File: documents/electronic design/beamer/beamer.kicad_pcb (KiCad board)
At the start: 2 copper layers, 28 parts, among them P1 CONN_01X20, P2 CONN_01X20, P3 CONN_01X02, P4 CONN_01X01, P5 CONN_01X01, T1 2N7002K, T10 2N7002K, T2 2N7002K, T3 2N7002K, T4 2N7002K, T5 2N7002K, T6 2N7002K, T7 2N7002K, T8 2N7002K, T9 2N7002K, U1 NRF24L01-BRKOUT, U2 74HC595D

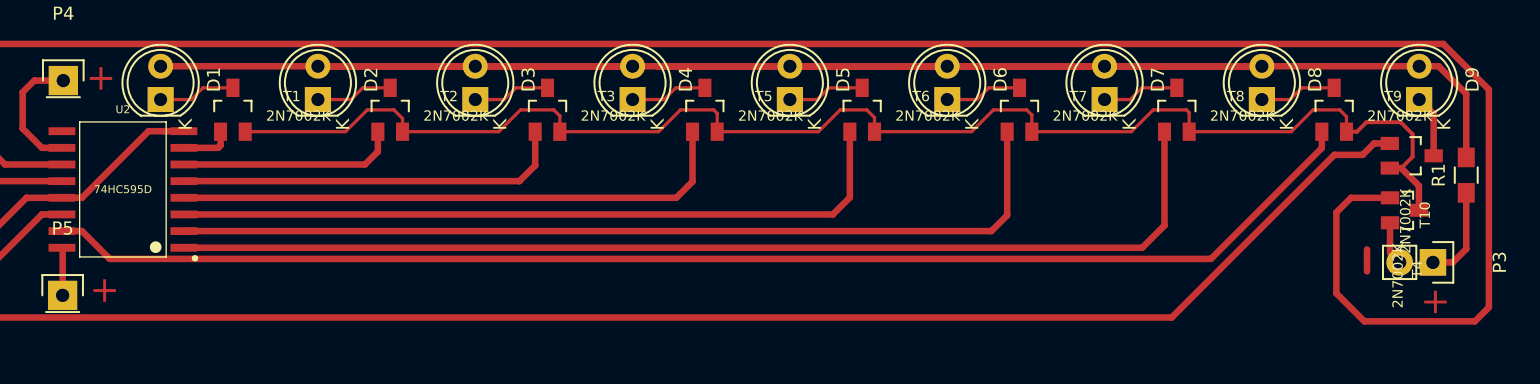
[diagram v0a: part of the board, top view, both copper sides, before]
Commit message: update pcb for beamer with shift registar
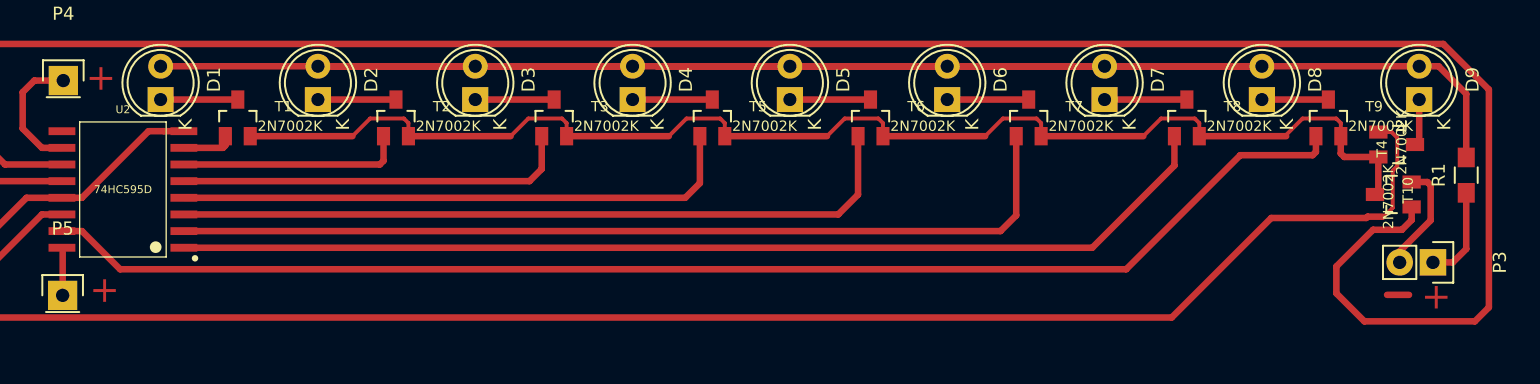
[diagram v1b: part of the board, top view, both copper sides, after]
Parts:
- T1, T10, T2, T3, T5, T6, T7, T8, T9: footprint sot23_modified:SOT23Mod -> sot23_modified:SOT23
- T4: footprint 2N7002K:SOT23 -> sot23_modified:SOT23
- moved T10 1.56 mm to (203.2, 58.4)
- moved T4 1.41 mm to (203.2, 62.2), turned to 90 degrees
- moved T8 1.09 mm to (187.3, 56.5)
- moved T7 1.04 mm to (175.3, 56.5)
- moved T6 1.00 mm to (163.2, 56.5)
- moved T5 0.96 mm to (151.1, 56.5)
- moved T3 0.93 mm to (139.1, 56.5)
- moved T2 0.89 mm to (127.0, 56.5)
- moved T9 0.89 mm to (198.1, 56.5)
- moved T1 0.86 mm to (114.9, 56.5)
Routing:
- net IR_PIN_ID: track 201.8 -> 207.2 mm
- net GND: track 71.7 -> 76.8 mm
- net Net-(T1-Pad2): track 112.0 -> 109.0 mm
- net IR_PIN_7: track 82.7 -> 80.4 mm
- net Net-(D9-Pad1): track 4.75 -> 3.57 mm
- net Net-(D8-Pad1): track 5.88 -> 5.07 mm
- net IR_PIN_2: track 16.7 -> 17.2 mm
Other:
- net class Default: clearance 0.3 -> 0.5
- rule trace_clearance: 0.3 -> 0.5

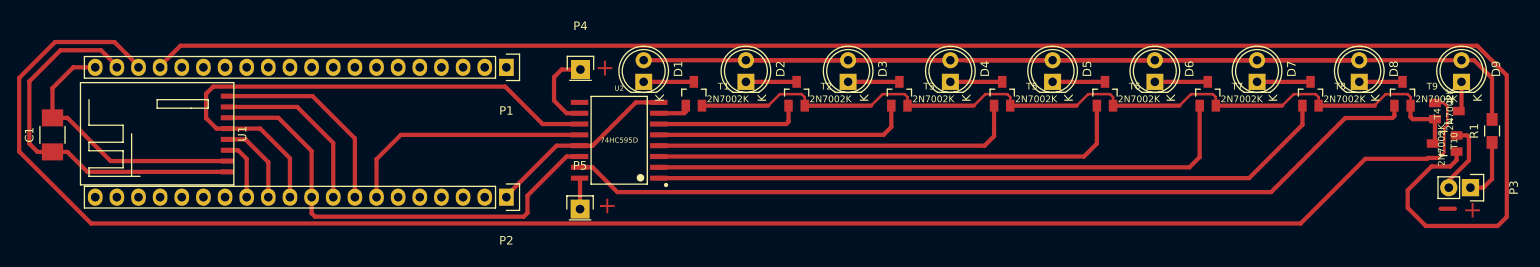
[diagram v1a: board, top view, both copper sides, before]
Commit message: update PCB for beamer, fix pin assignment for radiomodule
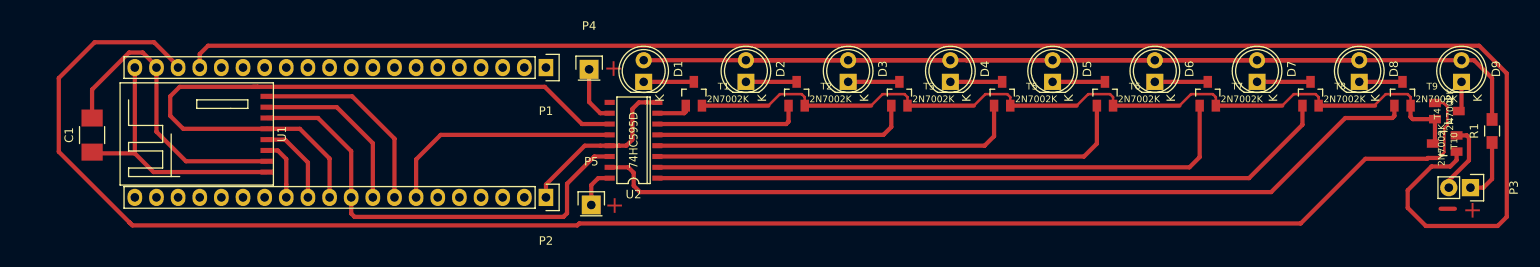
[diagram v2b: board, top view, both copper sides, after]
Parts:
- U2: footprint SOIC127P1030X265-16N:SOIC127P1030X265-16N -> 74HC595:SO16
- moved C1 4.65 mm to (44.3, 61.2)
- moved U1 4.65 mm to (65.6, 67.1)
- moved P1 4.65 mm to (97.6, 53.3)
- moved P2 4.65 mm to (97.6, 68.6)
- moved U2 1.68 mm to (107.9, 61.8), turned to 90 degrees
- moved P5 1.41 mm to (102.9, 69.4)
- moved P4 1.02 mm to (102.6, 53.5)
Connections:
- C1 pad 1: GND -> +3V3
- C1 pad 2: +3V3 -> GND
- U1 pad 1: GND -> +3V3
- U1 pad 2: +3V3 -> GND
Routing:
- net SPI1_SCK: track 65.2 -> 82.1 mm
- net GND: track 76.8 -> 66.1 mm
- net IR_PIN_ID: track 207.2 -> 203.0 mm
- net PWM_38K: track 200.5 -> 197.0 mm
- net IR_PIN_8: track 101.8 -> 99.1 mm
- net +3V3: track 52.9 -> 50.4 mm
- net ShiftReg_Expose: track 29.5 -> 28.4 mm

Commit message: minor update in beamer pcb layout
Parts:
- C1: footprint Capacitors_SMD:C_1210_HandSoldering -> Capacitors_SMD:C_0402
- moved C1 22.4 mm to (66.5, 64.4)
- moved P1 1.37 mm to (98.8, 52.8)
- moved P2 1.37 mm to (98.8, 68.0)
- moved P4 0.96 mm to (103.5, 53.0)
- moved P5 0.95 mm to (103.6, 68.8)
- moved U1 0.60 mm to (65.8, 66.5)
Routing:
- net IR_PIN_ID: track 203.0 -> 190.7 mm
- net +3V3: track 50.4 -> 43.2 mm
- net NRF_IRQ1: track 23.9 -> 27.3 mm
- net SPI1_MISO: track 20.5 -> 23.2 mm
- net PWM_38K: track 197.0 -> 194.5 mm
- net SPI1_SCK: track 82.1 -> 84.2 mm
- net SPI1_MOSI: track 54.3 -> 56.3 mm
- net NRF_CSN1: track 10.0 -> 12.0 mm
- net NRF_CE1: track 7.35 -> 8.67 mm
- net ShiftReg_Expose: track 28.4 -> 27.3 mm
- net GND: track 66.1 -> 65.5 mm
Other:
- board text added: "."

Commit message: changes in pcb
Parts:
- moved D5 33.6 mm to (135.2, 29.5)
- moved D6 33.6 mm to (147.2, 29.5)
- moved D7 33.6 mm to (159.2, 29.5)
- moved D8 33.6 mm to (171.2, 29.5)
- moved D9 33.6 mm to (183.2, 29.5)
- moved R1 33.6 mm to (186.8, 35.2)
- moved C1 33.6 mm to (44.7, 38.9)
- moved D3 33.6 mm to (111.2, 29.5)
- moved D4 33.6 mm to (123.2, 29.5)
- moved P1 33.6 mm to (77.0, 27.2)
- moved P2 33.6 mm to (77.0, 42.5)
- moved P4 33.6 mm to (81.6, 27.5)
- moved T1 33.6 mm to (93.1, 31.0)
- moved D1 33.6 mm to (87.2, 29.5)
- moved D2 33.6 mm to (99.2, 29.5)
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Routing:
- net GND: track 65.5 -> 55.3 mm
- net +3V3: track 43.2 -> 46.4 mm
- net NRF_CE1: track 8.67 -> 11.0 mm
- net SPI1_MISO: track 23.2 -> 25.5 mm
- net NRF_CSN1: track 12.0 -> 14.3 mm
- net SPI1_MOSI: track 56.3 -> 58.6 mm
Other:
- net class Default: clearance 0.5 -> 0.6
- rule trace_clearance: 0.5 -> 0.6

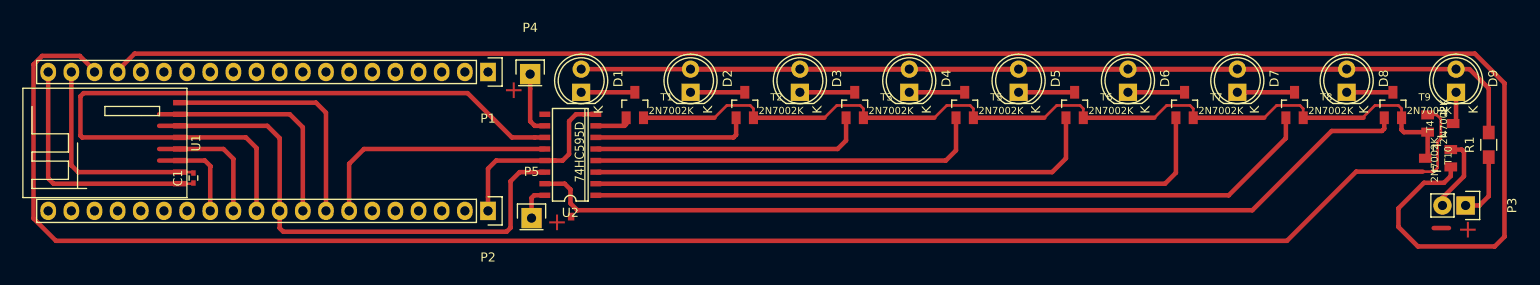
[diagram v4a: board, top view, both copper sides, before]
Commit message: update PCB for beamer
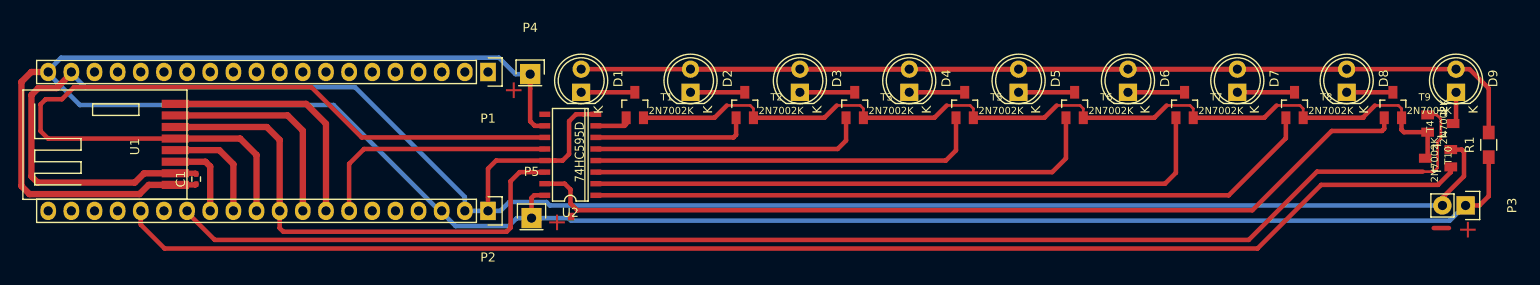
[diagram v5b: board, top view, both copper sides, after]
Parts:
- U1: footprint se8r01_smd:SE8R01_SMD -> SE8R01:se8r01_smd
- moved U1 1.09 mm to (45.0, 40.9)
- moved C1 0.32 mm to (45.0, 39.0)
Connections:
- P1 pad 17: PWM_38K -> Net-(P1-Pad17)
- P1 pad 18: IR_PIN_ID -> Net-(P1-Pad18)
- P2 pad 14: Net-(P2-Pad14) -> IR_PIN_ID
- P2 pad 16: Net-(P2-Pad16) -> PWM_38K
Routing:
- net +3V3: track 46.4 -> 271.2 mm
- net GND: track 55.3 -> 222.8 mm
- net PWM_38K: track 194.5 -> 150.4 mm
- net IR_PIN_ID: track 190.7 -> 149.4 mm
- net SPI1_SCK: track 84.2 -> 92.2 mm
- net NRF_CSN1: track 14.3 -> 12.1 mm
- net SPI1_MISO: track 25.5 -> 23.5 mm
- net SPI1_MOSI: track 58.6 -> 56.7 mm
- net NRF_CE1: track 11.0 -> 9.07 mm
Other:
- net class Default: clearance 0.6 -> 0.3
- rule trace_clearance: 0.6 -> 0.3

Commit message: save changes
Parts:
- removed the U1 at (45.0, 40.9)
- added C1: C, Capacitors_SMD:C_0402, F.Cu at (37.7, 64.8)
- added D1: LED, LEDs:LED-5MM, F.Cu at (79.9, 55.2)
- added D2: LED, LEDs:LED-5MM, F.Cu at (91.9, 55.2)
- added D3: LED, LEDs:LED-5MM, F.Cu at (103.9, 55.2)
- added D4: LED, LEDs:LED-5MM, F.Cu at (115.9, 55.2)
- added D5: LED, LEDs:LED-5MM, F.Cu at (127.9, 55.2)
- added D6: LED, LEDs:LED-5MM, F.Cu at (139.9, 55.2)
- added D7: LED, LEDs:LED-5MM, F.Cu at (151.9, 55.2)
- added D8: LED, LEDs:LED-5MM, F.Cu at (163.9, 55.2)
- added D9: LED, LEDs:LED-5MM, F.Cu at (175.9, 55.2)
- added P1: CONN_01X20, Socket_Strips:Socket_Strip_Straight_1x20, F.Cu at (69.7, 53.0)
- added P2: CONN_01X20, Socket_Strips:Socket_Strip_Straight_1x20, F.Cu at (69.7, 68.3)
- added P3: CONN_01X02, Pin_Headers:Pin_Header_Straight_1x02, F.Cu at (177.0, 67.7)
- added P4: CONN_01X01, Pin_Headers:Pin_Header_Straight_1x01, F.Cu at (74.3, 53.3)
- added P5: CONN_01X01, Pin_Headers:Pin_Header_Straight_1x01, F.Cu at (74.5, 69.1)
- added P6: CONN_01X08, Pin_Headers:Pin_Header_Straight_1x08, F.Cu at (265.6, 105.7)
- added P6: CONN_01X08, Pin_Headers:Pin_Header_Straight_1x08, F.Cu at (115.5, 133.8)
- added P6: CONN_01X08, Pin_Headers:Pin_Header_Straight_1x08, F.Cu at (266.2, 81.2)
- added P6: CONN_01X08, Pin_Headers:Pin_Header_Straight_1x08, F.Cu at (235.9, 105.7)
- added P6: CONN_01X08, Pin_Headers:Pin_Header_Straight_1x08, F.Cu at (236.5, 81.2)
- added P6: CONN_01X08, Pin_Headers:Pin_Header_Straight_1x08, F.Cu at (145.8, 109.2)
- added P6: CONN_01X08, Pin_Headers:Pin_Header_Straight_1x08, F.Cu at (175.9, 108.8)
- added P6: CONN_01X08, Pin_Headers:Pin_Header_Straight_1x08, F.Cu at (116.1, 109.2)
- added P6: CONN_01X08, Pin_Headers:Pin_Header_Straight_1x08, F.Cu at (175.3, 133.3)
- added P6: CONN_01X08, Pin_Headers:Pin_Header_Straight_1x08, F.Cu at (145.2, 133.8)
- added P7: CONN_01X04, Pin_Headers:Pin_Header_Straight_1x04, F.Cu at (203.9, 119.5)
- added P7: CONN_01X04, Pin_Headers:Pin_Header_Straight_1x04, F.Cu at (204.5, 94.9)
- added P7: CONN_01X04, Pin_Headers:Pin_Header_Straight_1x04, F.Cu at (32.6, 122.6)
- added P7: CONN_01X04, Pin_Headers:Pin_Header_Straight_1x04, F.Cu at (84.2, 123.0)
- added P7: CONN_01X04, Pin_Headers:Pin_Header_Straight_1x04, F.Cu at (58.1, 122.9)
- added P7: CONN_01X04, Pin_Headers:Pin_Header_Straight_1x04, F.Cu at (83.5, 147.6)
- added P7: CONN_01X04, Pin_Headers:Pin_Header_Straight_1x04, F.Cu at (57.5, 147.5)
- added P7: CONN_01X04, Pin_Headers:Pin_Header_Straight_1x04, F.Cu at (32.0, 147.2)
- added P8: CONN_01X08, Pin_Headers:Pin_Header_Straight_1x08, F.Cu at (248.0, 117.3)
- added P8: CONN_01X08, Pin_Headers:Pin_Header_Straight_1x08, F.Cu at (97.9, 145.3)
- added P8: CONN_01X08, Pin_Headers:Pin_Header_Straight_1x08, F.Cu at (248.6, 92.7)
- added P8: CONN_01X08, Pin_Headers:Pin_Header_Straight_1x08, F.Cu at (218.8, 92.7)
- added P8: CONN_01X08, Pin_Headers:Pin_Header_Straight_1x08, F.Cu at (218.2, 117.3)
- added P8: CONN_01X08, Pin_Headers:Pin_Header_Straight_1x08, F.Cu at (158.3, 120.3)
- added P8: CONN_01X08, Pin_Headers:Pin_Header_Straight_1x08, F.Cu at (128.2, 120.8)
- added P8: CONN_01X08, Pin_Headers:Pin_Header_Straight_1x08, F.Cu at (98.5, 120.8)
- added P8: CONN_01X08, Pin_Headers:Pin_Header_Straight_1x08, F.Cu at (157.7, 144.9)
- added P8: CONN_01X08, Pin_Headers:Pin_Header_Straight_1x08, F.Cu at (127.6, 145.3)
- added P9: CONN_01X04, Pin_Headers:Pin_Header_Straight_1x04, F.Cu at (197.5, 78.7)
- added P9: CONN_01X04, Pin_Headers:Pin_Header_Straight_1x04, F.Cu at (196.9, 103.3)
- added P9: CONN_01X04, Pin_Headers:Pin_Header_Straight_1x04, F.Cu at (25.6, 106.4)
- added P9: CONN_01X04, Pin_Headers:Pin_Header_Straight_1x04, F.Cu at (77.1, 106.8)
- added P9: CONN_01X04, Pin_Headers:Pin_Header_Straight_1x04, F.Cu at (51.1, 106.7)
- added P9: CONN_01X04, Pin_Headers:Pin_Header_Straight_1x04, F.Cu at (76.5, 131.4)
- added P9: CONN_01X04, Pin_Headers:Pin_Header_Straight_1x04, F.Cu at (50.5, 131.3)
- added P9: CONN_01X04, Pin_Headers:Pin_Header_Straight_1x04, F.Cu at (25.0, 131.0)
- added R1: R, Resistors_SMD:R_0805_HandSoldering, F.Cu at (179.5, 61.0)
- added T1: 2N7002K, sot23_modified:SOT23, F.Cu at (85.8, 56.8)
- added T10: 2N7002K, sot23_modified:SOT23, F.Cu at (174.1, 58.7)
- added T2: 2N7002K, sot23_modified:SOT23, F.Cu at (97.9, 56.8)
- added T3: 2N7002K, sot23_modified:SOT23, F.Cu at (110.0, 56.8)
- added T4: 2N7002K, sot23_modified:SOT23, F.Cu at (174.1, 62.5)
- added T5: 2N7002K, sot23_modified:SOT23, F.Cu at (122.0, 56.8)
- added T6: 2N7002K, sot23_modified:SOT23, F.Cu at (134.1, 56.8)
- added T7: 2N7002K, sot23_modified:SOT23, F.Cu at (146.2, 56.8)
- added T8: 2N7002K, sot23_modified:SOT23, F.Cu at (158.2, 56.8)
- added T9: 2N7002K, sot23_modified:SOT23, F.Cu at (169.0, 56.8)
- added U1: NRF24L01-BRKOUT, SE8R01:se8r01_smd, F.Cu at (209.6, 117.1)
- added U1: NRF24L01-BRKOUT, SE8R01:se8r01_smd, F.Cu at (210.2, 92.5)
- added U1: NRF24L01-BRKOUT, SE8R01:se8r01_smd, F.Cu at (38.2, 120.2)
- added U1: NRF24L01-BRKOUT, SE8R01:se8r01_smd, F.Cu at (89.8, 120.6)
- added U1: NRF24L01-BRKOUT, SE8R01:se8r01_smd, F.Cu at (63.8, 120.5)
- added U1: NRF24L01-BRKOUT, SE8R01:se8r01_smd, F.Cu at (89.2, 145.2)
- added U1: NRF24L01-BRKOUT, SE8R01:se8r01_smd, F.Cu at (63.2, 145.1)
- added U1: NRF24L01-BRKOUT, SE8R01:se8r01_smd, F.Cu at (37.6, 144.8)
- added U2: 74HC595D, 74HC595:SO16, F.Cu at (78.7, 62.1)
- added U3: 74HC595D, 74HC595:SO16, F.Cu at (256.6, 111.5)
- added U3: 74HC595D, 74HC595:SO16, F.Cu at (106.5, 139.6)
- added U3: 74HC595D, 74HC595:SO16, F.Cu at (257.2, 86.9)
- added U3: 74HC595D, 74HC595:SO16, F.Cu at (226.9, 111.5)
- added U3: 74HC595D, 74HC595:SO16, F.Cu at (227.5, 86.9)
- added U3: 74HC595D, 74HC595:SO16, F.Cu at (167.0, 114.5)
- added U3: 74HC595D, 74HC595:SO16, F.Cu at (136.9, 115.0)
- added U3: 74HC595D, 74HC595:SO16, F.Cu at (107.1, 115.0)
- added U3: 74HC595D, 74HC595:SO16, F.Cu at (166.4, 139.1)
- added U3: 74HC595D, 74HC595:SO16, F.Cu at (136.2, 139.6)
- added U4: NRF24L01-BRKOUT, SE8R01:se8r01_smd, F.Cu at (37.8, 66.7)
- added U4: NRF24L01-BRKOUT, SE8R01:se8r01_smd, F.Cu at (38.1, 94.6)
- moved R1 54.1 mm to (179.8, 88.9)
- moved C1 54.1 mm to (38.0, 92.7)
- moved P2 54.1 mm to (70.0, 96.1)
- moved P3 54.1 mm to (177.3, 95.6)
- moved P5 54.1 mm to (74.8, 96.9)
- moved D1 54.1 mm to (80.2, 83.1)
- moved D2 54.1 mm to (92.2, 83.1)
- moved D3 54.1 mm to (104.2, 83.1)
- moved D4 54.1 mm to (116.2, 83.1)
- moved D5 54.1 mm to (128.2, 83.1)
- moved D6 54.1 mm to (140.2, 83.1)
- moved D7 54.1 mm to (152.2, 83.1)
- moved D8 54.1 mm to (164.2, 83.1)
- moved D9 54.1 mm to (176.2, 83.1)
- moved P1 54.1 mm to (70.0, 80.9)
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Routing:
- net +3V3: track 271.2 -> 542.5 mm
- net GND: track 222.8 -> 445.7 mm
- net Net-(D1-Pad2): track 175.8 -> 351.6 mm
- net PWM_38K: track 150.4 -> 300.8 mm
- net IR_PIN_ID: track 149.4 -> 298.8 mm
- net Net-(P7-Pad4): track 0.00 -> 128.5 mm
- net Net-(P9-Pad1): track 0.00 -> 127.2 mm
- net Net-(T1-Pad2): track 109.0 -> 218.0 mm
- net Net-(P7-Pad3): track 0.00 -> 104.5 mm
- net Net-(P9-Pad2): track 0.00 -> 103.9 mm
- net IR_PIN_8: track 99.1 -> 198.2 mm
- net SPI1_SCK: track 92.2 -> 184.5 mm
- net IR_PIN_7: track 80.4 -> 160.8 mm
- net Net-(P7-Pad2): track 0.00 -> 80.0 mm
- net Net-(P9-Pad3): track 0.00 -> 74.6 mm
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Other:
- net class Default: trace_width 0.5 -> 0.4

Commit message: make new project for beamer
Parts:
- removed the C1 at (38.0, 92.7)
- removed the D1 at (80.2, 83.1)
- removed the D2 at (92.2, 83.1)
- removed the D3 at (104.2, 83.1)
- removed the D4 at (116.2, 83.1)
- removed the D5 at (128.2, 83.1)
- removed the D6 at (140.2, 83.1)
- removed the D7 at (152.2, 83.1)
- removed the D8 at (164.2, 83.1)
- removed the D9 at (176.2, 83.1)
- removed the P1 at (70.0, 80.9)
- removed the P2 at (70.0, 96.1)
- removed the P3 at (177.3, 95.6)
- removed the P4 at (74.6, 81.1)
- removed the P5 at (74.8, 96.9)
- removed the P6 at (265.6, 105.7)
- removed the P6 at (115.5, 133.8)
- removed the P6 at (266.2, 81.2)
- removed the P6 at (235.9, 105.7)
- removed the P6 at (236.5, 81.2)
- removed the P6 at (145.8, 109.2)
- removed the P6 at (175.9, 108.8)
- removed the P6 at (116.1, 109.2)
- removed the P6 at (145.2, 133.8)
- removed the P7 at (203.9, 119.5)
- removed the P7 at (204.5, 94.9)
- removed the P7 at (32.6, 122.6)
- removed the P7 at (84.2, 123.0)
- removed the P7 at (58.1, 122.9)
- removed the P7 at (83.5, 147.6)
- removed the P7 at (57.5, 147.5)
- removed the P8 at (248.0, 117.3)
- removed the P8 at (97.9, 145.3)
- removed the P8 at (248.6, 92.7)
- removed the P8 at (218.8, 92.7)
- removed the P8 at (218.2, 117.3)
- removed the P8 at (158.3, 120.3)
- removed the P8 at (128.2, 120.8)
- removed the P8 at (98.5, 120.8)
- removed the P8 at (127.6, 145.3)
- removed the P9 at (197.5, 78.7)
- removed the P9 at (196.9, 103.3)
- removed the P9 at (25.6, 106.4)
- removed the P9 at (77.1, 106.8)
- removed the P9 at (51.1, 106.7)
- removed the P9 at (76.5, 131.4)
- removed the P9 at (50.5, 131.3)
- removed the R1 at (179.8, 88.9)
- removed the T1 at (86.1, 84.7)
- removed the T10 at (174.4, 86.6)
- removed the T2 at (98.2, 84.7)
- removed the T3 at (110.3, 84.7)
- removed the T4 at (174.4, 90.4)
- removed the T5 at (122.3, 84.7)
- removed the T6 at (134.4, 84.7)
- removed the T7 at (146.5, 84.7)
- removed the T8 at (158.5, 84.7)
- removed the T9 at (169.3, 84.7)
- removed the U1 at (209.6, 117.1)
- removed the U1 at (210.2, 92.5)
- removed the U1 at (38.2, 120.2)
- removed the U1 at (89.8, 120.6)
- removed the U1 at (63.8, 120.5)
- removed the U1 at (89.2, 145.2)
- removed the U1 at (63.2, 145.1)
- removed the U2 at (79.1, 90.0)
- removed the U3 at (256.6, 111.5)
- removed the U3 at (106.5, 139.6)
- removed the U3 at (257.2, 86.9)
- removed the U3 at (226.9, 111.5)
- removed the U3 at (227.5, 86.9)
- removed the U3 at (167.0, 114.5)
- removed the U3 at (136.9, 115.0)
- removed the U3 at (107.1, 115.0)
- removed the U3 at (136.2, 139.6)
- removed the U4 at (38.1, 94.6)
- moved U3 85.2 mm to (91.6, 98.3)
- moved P6 85.2 mm to (100.6, 92.5)
- moved P8 85.2 mm to (82.9, 104.1)
- moved P9 42.1 mm to (37.3, 90.7)
- moved U1 42.1 mm to (49.9, 104.5)
- moved P7 42.1 mm to (44.3, 106.9)
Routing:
- net +3V3: track 542.5 -> 271.2 mm
- net GND: track 445.7 -> 222.8 mm
- net Net-(D1-Pad2): track 351.6 -> 175.8 mm
- net PWM_38K: track 300.8 -> 150.4 mm
- net IR_PIN_ID: track 298.8 -> 149.4 mm
- net Net-(P7-Pad4): track 128.5 -> 16.1 mm
- net Net-(P9-Pad1): track 127.2 -> 15.9 mm
- net Net-(T1-Pad2): track 218.0 -> 109.0 mm
- net IR_PIN_8: track 198.2 -> 99.1 mm
- net SPI1_SCK: track 184.5 -> 92.2 mm
- net Net-(P7-Pad3): track 104.5 -> 13.1 mm
- net Net-(P9-Pad2): track 103.9 -> 13.0 mm
- net IR_PIN_7: track 160.8 -> 80.4 mm
- net IR_PIN_6: track 140.1 -> 70.0 mm
- net Net-(P7-Pad2): track 80.0 -> 10.00 mm
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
